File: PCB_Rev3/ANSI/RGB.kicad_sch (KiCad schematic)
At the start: 61 parts

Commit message: Add files via upload
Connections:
- net VBUS renamed RGB
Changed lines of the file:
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@@
 		(on_board yes)
 		(dnp no)
-		(fields_autoplaced yes)
 		(property "Reference" "#PWR035"
 			(at 29.21 124.46 0)
@@
 			)
 		)
-		(property "Value" "VBUS"
-			(at 29.21 133.35 0)
+		(property "Value" "RGB"
+			(at 32.004 127.254 0)
 			(effects
 				(font
 					(size 1.27 1.27)
 				)
+				(justify right)
 			)
 		)

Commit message: Finish board design
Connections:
- net RGB renamed VBUS_SW
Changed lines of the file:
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@@
 			)
 		)
-		(property "Value" "RGB"
+		(property "Value" "VBUS_SW"
 			(at 32.004 127.254 0)
 			(effects

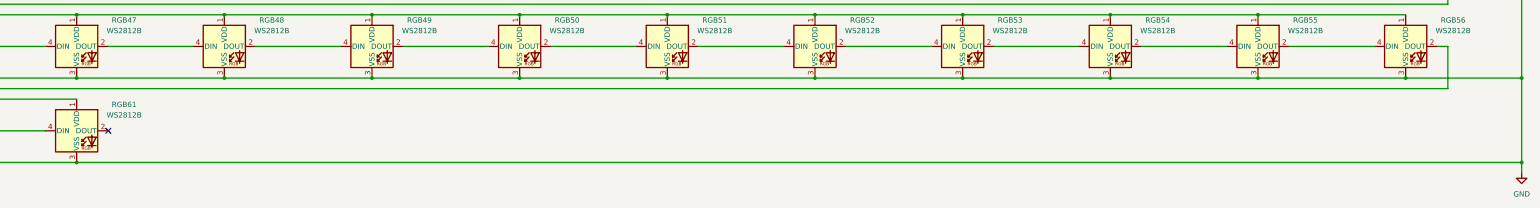
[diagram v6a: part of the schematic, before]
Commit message: More stabilization circuit
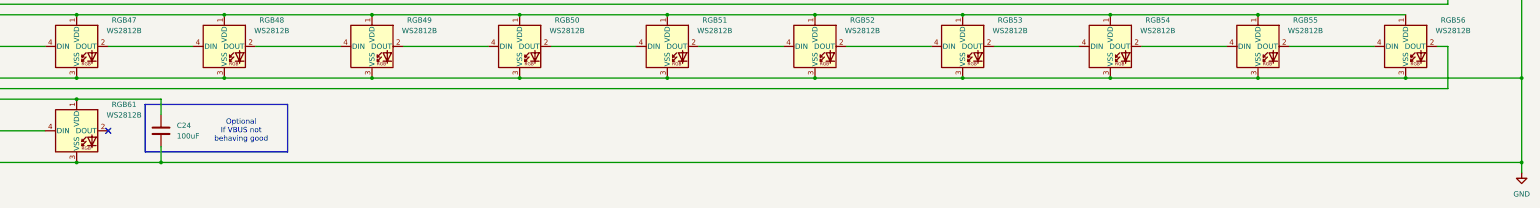
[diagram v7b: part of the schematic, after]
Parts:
- added C24: 100uF, Capacitor_SMD:C_1206_3216Metric, symbol Device:C
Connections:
- net GND: now also C24.2
- net VBUS_SW: now also C24.1
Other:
- note added: "Optional If VBUS not behaving good"
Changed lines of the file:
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@@
 	(generator_version "9.0")
 	(paper "A2")
+	(rectangle
+		(start 200.66 111.76)
+		(end 234.95 123.19)
+		(stroke
+			(width 0)
+			(type default)
+		)
+		(fill
+			(type none)
+		)
+	)
+	(text "Optional\nIf VBUS not\nbehaving good"
+		(exclude_from_sim no)
+		(at 223.774 118.11 0)
+		(effects
+			(font
+				(size 1.27 1.27)
+			)
+		)
+	)
 	(junction
 		(at 77.47 44.45)
@@
 	)
 	(junction
+		(at 184.15 110.49)
+		(diameter 0)
+		(color 0 0 0 0)
+	)
+	(junction
 		(at 468.63 90.17)
 		(diameter 0)
@@
 	)
 	(junction
+		(at 204.47 125.73)
+		(diameter 0)
+		(color 0 0 0 0)
+	)
+	(junction
 		(at 504.19 29.21)
 		(diameter 0)
@@
 	(wire
 		(pts
-			(xy 184.15 125.73) (xy 532.13 125.73)
+			(xy 184.15 125.73) (xy 204.47 125.73)
 		)
 		(stroke
@@
 	(wire
 		(pts
+			(xy 184.15 110.49) (xy 204.47 110.49)
+		)
+		(stroke
+			(width 0)
+			(type default)
+		)
+	)
+	(wire
+		(pts
 			(xy 468.63 64.77) (xy 504.19 64.77)
 		)
@@
 	(wire
 		(pts
+			(xy 204.47 110.49) (xy 204.47 114.3)
+		)
+		(stroke
+			(width 0)
+			(type default)
+		)
+	)
+	(wire
+		(pts
 			(xy 49.53 57.15) (xy 69.85 57.15)
 		)
@@
 	(wire
 		(pts
+			(xy 204.47 125.73) (xy 532.13 125.73)
+		)
+		(stroke
+			(width 0)
+			(type default)
+		)
+	)
+	(wire
+		(pts
 			(xy 468.63 29.21) (xy 504.19 29.21)
 		)
@@
 	(wire
 		(pts
+			(xy 204.47 121.92) (xy 204.47 125.73)
+		)
+		(stroke
+			(width 0)
+			(type default)
+		)
+	)
+	(wire
+		(pts
 			(xy 369.57 97.79) (xy 389.89 97.79)
 		)
@@
 					(unit 1)
 				)
+			)
+		)
+	)
+	(symbol
+		(lib_id "Device:C")
+		(at 204.47 118.11 0)
+		(unit 1)
+		(exclude_from_sim no)
+		(in_bom no)
+		(on_board yes)
+		(dnp no)
+		(fields_autoplaced yes)
+		(property "Reference" "C24"
+			(at 208.28 116.8399 0)
+			(effects
+				(font
+					(size 1.27 1.27)
+				)
+				(justify left)
+			)
+		)
+		(property "Value" "100uF"
+			(at 208.28 119.3799 0)
+			(effects
+				(font
+					(size 1.27 1.27)
+				)
+				(justify left)
+			)
+		)
+		(property "Footprint" "Capacitor_SMD:C_1206_3216Metric"
+			(at 205.4352 121.92 0)
+			(effects
+				(font
+					(size 1.27 1.27)
+				)
+				(hide yes)
+			)
+		)
+		(property "Datasheet" "~"
+			(at 204.47 118.11 0)
+			(effects
+				(font
+					(size 1.27 1.27)
+				)
+				(hide yes)
+			)
+		)
+		(property "Description" "Unpolarized capacitor"
+			(at 204.47 118.11 0)
+			(effects
+				(font
+					(size 1.27 1.27)
+				)
+				(hide yes)
+			)
+		)
+		(pin "2"
+		)
+		(pin "1"
+		)
+		(instances
+			(project ""
+				(path "/dca0f898-8fdb-4522-a51d-f4f4238906e7/c0337f82-e68f-485d-b406-18ae8e593971"
+					(reference "C24")
+					(unit 1)
+				)

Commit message: vbus layout
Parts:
- added C25, C26: 100uF, Capacitor_SMD:C_1206_3216Metric, symbol Device:C
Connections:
- net GND: now also C25.2, C26.2
- net VBUS_SW: now also C25.1, C26.1
- net at RGB29.4 (DIN): now also RGB15.4 (DIN); no longer RGB28.2 (DOUT)
- net rgb1: now reaches RGB54.4 (DIN)
- net rgb1: now also RGB42.2 (DOUT); no longer RGB53.2 (DOUT)
- net rgb4: now reaches RGB56.2 (DOUT), RGB57.4 (DIN)
- net at RGB14.2 (DOUT): now also RGB28.2 (DOUT); no longer RGB15.4 (DIN)
- net rgb2: now reaches RGB42.4 (DIN)
- net rgb2: now also RGB43.4 (DIN); no longer RGB41.2 (DOUT)
- new net rgb3: RGB41.2 (DOUT), RGB53.2 (DOUT)
